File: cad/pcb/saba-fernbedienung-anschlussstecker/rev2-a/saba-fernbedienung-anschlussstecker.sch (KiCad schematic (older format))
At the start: 7 parts, among them J101 Conn_01x04, J102 Conn_01x04, J103 Conn_01x04, J104 Conn_01x02, J105 Conn_01x04, J106 Conn_01x04, X101 Stecker-6-3D

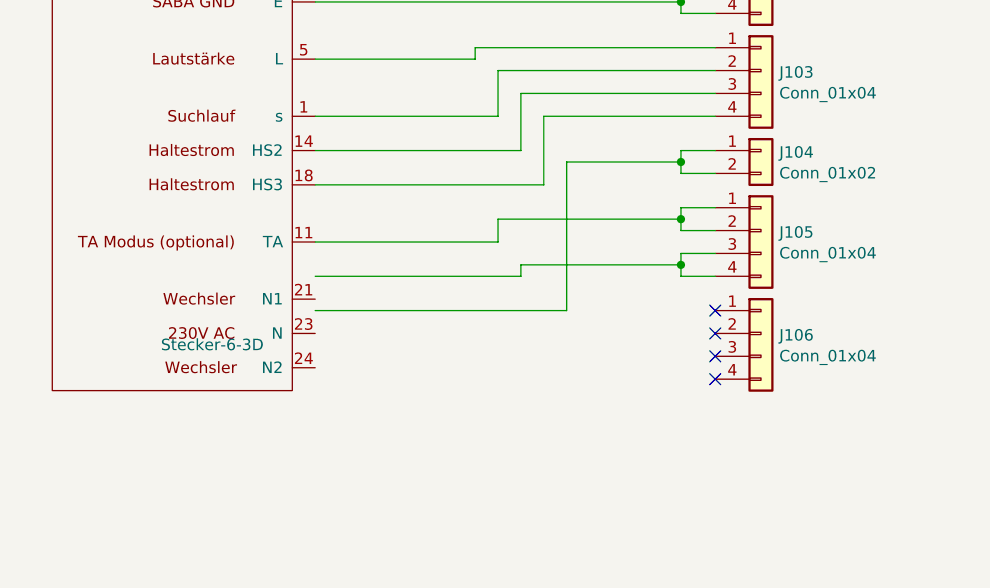
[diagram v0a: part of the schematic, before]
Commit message: Fix: Stecker
- Durchmesser Mittelloch groesser
- Position Befestigungsloch weiter rechts
- Position Pin15 korrigiert
- Pin11 hinzugefuegt. Ist in der Steckdose nicht belegt.
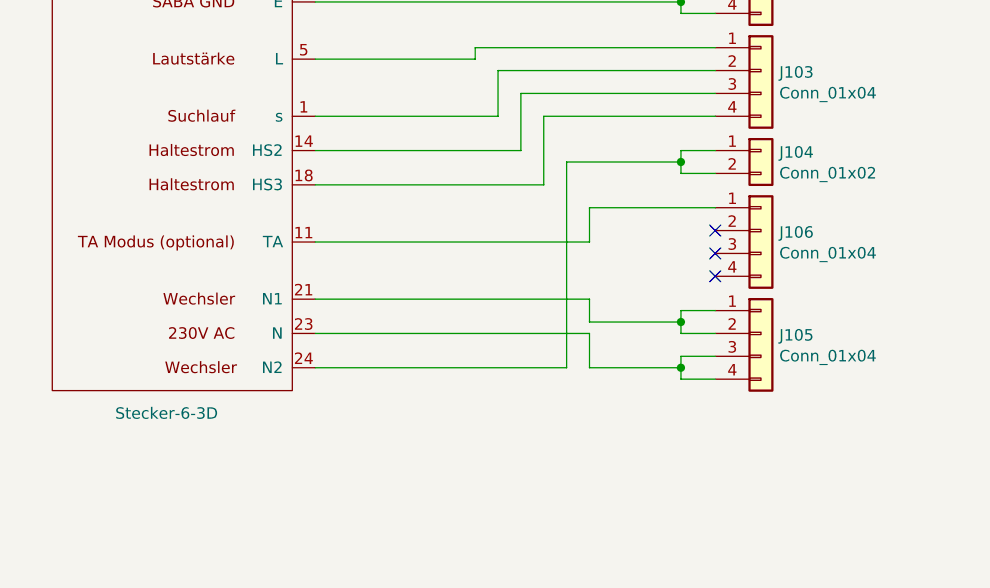
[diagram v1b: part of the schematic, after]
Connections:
- wire segments 49 -> 52
- no-connect marks 4 -> 3
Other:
- moved on the sheet: J105, J106
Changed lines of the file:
@@
 P 2350 2850
 F 0 "X101" H 2500 3650 50  0000 C CNN
-F 1 "Stecker-6-3D" H 2500 1300 50  0000 C CNN
+F 1 "Stecker-6-3D" H 2700 1000 50  0000 C CNN
 F 2 "stecker:stecker-6-3d" H 2350 2700 50  0001 C CNN
 F 3 "" H 2350 2700 50  0001 C CNN
@@
 L Connector_Generic:Conn_01x04 J105
 U 1 1 5FFBFD33
-P 4600 3900
-F 0 "J105" H 4680 3892 50  0000 L CNN
-F 1 "Conn_01x04" H 4680 3801 50  0000 L CNN
-F 2 "Connector_PinHeader_2.54mm:PinHeader_1x04_P2.54mm_Vertical" H 4600 3900 50  0001 C CNN
-F 3 "~" H 4600 3900 50  0001 C CNN
-	1    4600 3900
-	1    0    0    -1
-$EndComp
-Wire Wire Line
-	4250 2350 4250 2300
-Wire Wire Line
-	4250 2300 4400 2300
-Wire Wire Line
-	4400 2400 4250 2400
-Wire Wire Line
-	4250 2400 4250 2350
-Connection ~ 4250 2350
-Wire Wire Line
-	2650 2500 4400 2500
-Wire Wire Line
-	2650 2350 4250 2350
-Wire Wire Line
-	2650 2200 4400 2200
-Wire Wire Line
-	2650 2750 4250 2750
-Wire Wire Line
-	4250 2750 4250 2650
-Wire Wire Line
-	4250 2650 4400 2650
-Wire Wire Line
-	4400 2750 4250 2750
-Connection ~ 4250 2750
-Wire Wire Line
-	2650 2900 4250 2900
-Wire Wire Line
-	4400 2950 4250 2950
-Wire Wire Line
-	4250 2950 4250 2900
-Wire Wire Line
-	4400 2850 4250 2850
-Wire Wire Line
-	4250 2850 4250 2900
-Connection ~ 4250 2900
-Wire Wire Line
-	2650 3150 3350 3150
-Wire Wire Line
-	3350 3150 3350 3100
-Wire Wire Line
-	3350 3100 4400 3100
-Wire Wire Line
-	2650 3400 3450 3400
-Wire Wire Line
-	3450 3400 3450 3200
-Wire Wire Line
-	3450 3200 4400 3200
-Wire Wire Line
-	2650 3550 3550 3550
-Wire Wire Line
-	3550 3550 3550 3300
-Wire Wire Line
-	3550 3300 4400 3300
-Wire Wire Line
-	2650 3700 3650 3700
-Wire Wire Line
-	3650 3700 3650 3400
-Wire Wire Line
-	3650 3400 4400 3400
-Wire Wire Line
-	4400 3900 4250 3900
-$Comp
-L Connector_Generic:Conn_01x04 J106
-U 1 1 5FFD7E5D
 P 4600 4350
-F 0 "J106" H 4680 4342 50  0000 L CNN
+F 0 "J105" H 4680 4342 50  0000 L CNN
 F 1 "Conn_01x04" H 4680 4251 50  0000 L CNN
 F 2 "Connector_PinHeader_2.54mm:PinHeader_1x04_P2.54mm_Vertical" H 4600 4350 50  0001 C CNN
@@
 $EndComp
 Wire Wire Line
-	4250 3800 4400 3800
-NoConn ~ 4400 4250
-NoConn ~ 4400 4350
-NoConn ~ 4400 4450
-NoConn ~ 4400 4550
+	4250 2350 4250 2300
+Wire Wire Line
+	4250 2300 4400 2300
+Wire Wire Line
+	4400 2400 4250 2400
+Wire Wire Line
+	4250 2400 4250 2350
+Connection ~ 4250 2350
+Wire Wire Line
+	2650 2500 4400 2500
+Wire Wire Line
+	2650 2350 4250 2350
+Wire Wire Line
+	2650 2200 4400 2200
+Wire Wire Line
+	2650 2750 4250 2750
+Wire Wire Line
+	4250 2750 4250 2650
+Wire Wire Line
+	4250 2650 4400 2650
+Wire Wire Line
+	4400 2750 4250 2750
+Connection ~ 4250 2750
+Wire Wire Line
+	2650 2900 4250 2900
+Wire Wire Line
+	4400 2950 4250 2950
+Wire Wire Line
+	4250 2950 4250 2900
+Wire Wire Line
+	4400 2850 4250 2850
+Wire Wire Line
+	4250 2850 4250 2900
+Connection ~ 4250 2900
+Wire Wire Line
+	2650 3150 3350 3150
+Wire Wire Line
+	3350 3150 3350 3100
+Wire Wire Line
+	3350 3100 4400 3100
+Wire Wire Line
+	2650 3400 3450 3400
+Wire Wire Line
+	3450 3400 3450 3200
+Wire Wire Line
+	3450 3200 4400 3200
+Wire Wire Line
+	2650 3550 3550 3550
+Wire Wire Line
+	3550 3550 3550 3300
+Wire Wire Line
+	3550 3300 4400 3300
+Wire Wire Line
+	2650 3700 3650 3700
+Wire Wire Line
+	3650 3700 3650 3400
+Wire Wire Line
+	3650 3400 4400 3400
+Wire Wire Line
+	4400 4350 4250 4350
+Wire Wire Line
+	4250 4250 4400 4250
+NoConn ~ 4400 3900
+NoConn ~ 4400 4000
+NoConn ~ 4400 4100
 Text Notes 1350 1850 0    118  ~ 0
 Anschluss Saba Stecker -> 2,54mm Pinheader
@@
 $EndComp
 Wire Wire Line
-	4250 4000 4400 4000
-Wire Wire Line
-	4400 4100 4250 4100
+	4250 4450 4400 4450
+Wire Wire Line
+	4400 4550 4250 4550
 $Comp
 L Connector_Generic:Conn_01x02 J104
@@
 $EndComp
 Wire Wire Line
-	2650 4250 3750 4250
-Wire Wire Line
-	3750 4250 3750 3600
-Wire Wire Line
 	3750 3600 4250 3600
 Wire Wire Line
@@
 	4250 3650 4250 3600
 Connection ~ 4250 3600
-Wire Wire Line
-	2650 3950 3450 3950
-Wire Wire Line
-	4250 3800 4250 3850
-Wire Wire Line
-	4250 4000 4250 4050
-Wire Wire Line
-	3450 3950 3450 3850
-Wire Wire Line
-	3450 3850 4250 3850
-Connection ~ 4250 3850
-Wire Wire Line
-	4250 3850 4250 3900
-Wire Wire Line
-	3550 4100 3550 4050
-Wire Wire Line
-	3550 4050 4250 4050
-Wire Wire Line
-	2650 4100 3550 4100
-Connection ~ 4250 4050
-Wire Wire Line
-	4250 4050 4250 4100
+$Comp
+L Connector_Generic:Conn_01x04 J106
+U 1 1 5FFD7E5D
+P 4600 3900
+F 0 "J106" H 4680 3892 50  0000 L CNN
+F 1 "Conn_01x04" H 4680 3801 50  0000 L CNN
+F 2 "Connector_PinHeader_2.54mm:PinHeader_1x04_P2.54mm_Vertical" H 4600 3900 50  0001 C CNN
+F 3 "~" H 4600 3900 50  0001 C CNN
+	1    4600 3900
+	1    0    0    -1
+$EndComp
+Wire Wire Line
+	4250 4450 4250 4500
+Wire Wire Line
+	4250 4250 4250 4300
+Wire Wire Line
+	3750 3600 3750 4500
+Wire Wire Line
+	3750 4500 2650 4500
+Wire Wire Line
+	2650 4350 3850 4350
+Wire Wire Line
+	3850 4350 3850 4500
+Wire Wire Line
+	3850 4500 4250 4500
+Connection ~ 4250 4500
+Wire Wire Line
+	4250 4500 4250 4550
+Wire Wire Line
+	4250 4300 3850 4300
+Wire Wire Line
+	3850 4300 3850 4200
+Wire Wire Line
+	3850 4200 2650 4200
+Connection ~ 4250 4300
+Wire Wire Line
+	4250 4300 4250 4350
+Wire Wire Line
+	3850 3800 3850 3950
+Wire Wire Line
+	3850 3950 2650 3950
+Wire Wire Line
+	4400 3800 3850 3800
 $EndSCHEMATC
